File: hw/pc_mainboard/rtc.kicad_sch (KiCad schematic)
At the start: 1 part, among them U5 MCP7940MT-I/SN

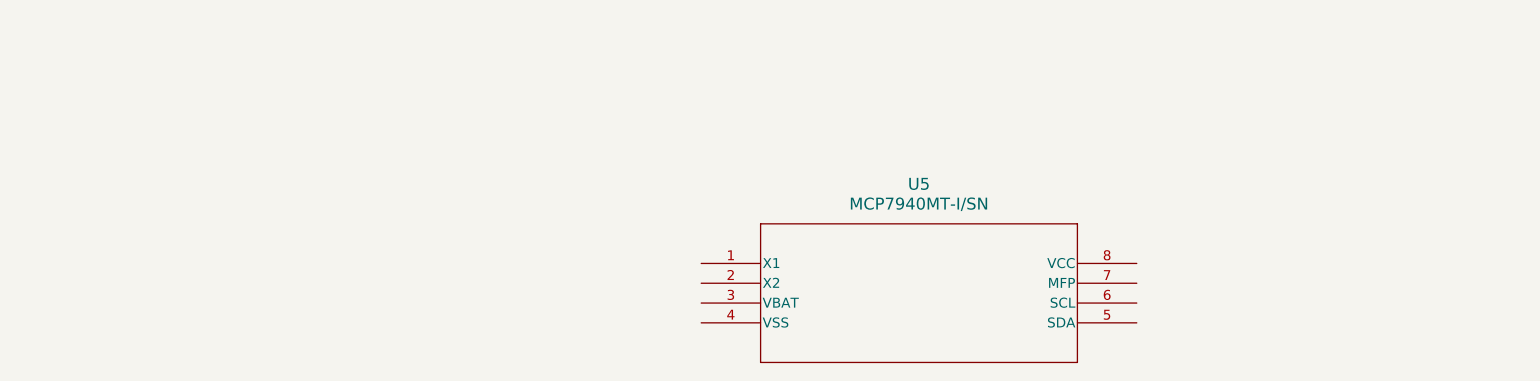
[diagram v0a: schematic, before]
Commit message: RTC Schematic Capture (#35)
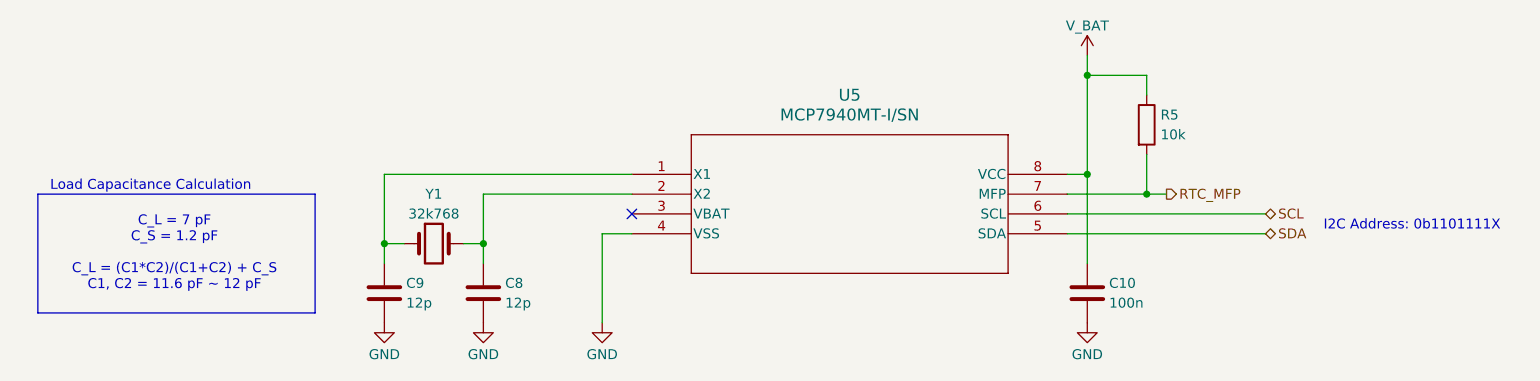
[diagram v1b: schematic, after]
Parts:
- added C10: 100n, symbol Device:C
- added C8, C9: 12p, symbol Device:C
- added R5: 10k, symbol Device:R
- added Y1: 32k768, symbol Device:Crystal
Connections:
- net at U5.1 (X1): now also C9.1, Y1.1
- net at U5.2 (X2): now also C8.1, Y1.2
- net GND: now reaches U5.4 (VSS)
- net GND: now also C10.2, C8.2, C9.2
- net SDA: now reaches U5.5 (SDA)
- net SCL: now reaches U5.6 (SCL)
- net RTC_MFP: now reaches U5.7 (MFP)
- net RTC_MFP: now also R5.2
- net V_BAT: now reaches U5.8 (VCC)
- net V_BAT: now also C10.1, R5.1
- no-connect marks 0 -> 1
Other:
- note added: "C_L = 7 pF C_S = 1.2 pF C_L = (C1*C2)/(C1+C2) + C_S C1, C2 = 11.6 pF ~ 12 pF"
- note added: "I2C Address: 0b1101111X"
- note added: "Load Capacitance Calculation"
- moved on the sheet: U5

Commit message: EEPROM Research (#36)
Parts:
- removed U5: MCP7940MT-I/SN, SOIC8-N_MC_MCH, symbol pc_mainboard:MCP7940MT-I_SN
- added U5: MCP7940MT-I/SN, SOIC8-N_MC_MCH, symbol pc_mainboard:rtc_MCP7940MT-I_SN
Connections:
- net GND: now also U5.4 (VSS)
- net RTC_MFP: now also U5.7 (MFP)
- net SCL: now also U5.6 (SCL)
- net SDA: now also U5.5 (SDA)
- net V_BAT: now also U5.8 (VCC)
- net at C9.1, Y1.1: now also U5.1 (X1)
- net at C8.1, Y1.2: now also U5.2 (X2)
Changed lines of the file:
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@@
+	)
+	(symbol
+		(lib_id "pc_mainboard:rtc_MCP7940MT-I_SN")
+		(at 119.38 88.9 0)
+		(unit 1)
+		(exclude_from_sim no)
+		(in_bom yes)
+		(on_board yes)
+		(dnp no)
+		(fields_autoplaced yes)
+		(property "Reference" "U5"
+			(at 147.32 78.74 0)
+			(effects
+				(font
+					(size 1.524 1.524)
+				)
+			)
+		)
+		(property "Value" "MCP7940MT-I/SN"
+			(at 147.32 81.28 0)
+			(effects
+				(font
+					(size 1.524 1.524)
+				)
+			)
+		)
+		(property "Footprint" "SOIC8-N_MC_MCH"
+			(at 119.38 88.9 0)
+			(effects
+				(font
+					(size 1.27 1.27)
+					(italic yes)
+				)
+				(hide yes)
+			)
+		)
+		(property "Datasheet" "MCP7940MT-I/SN"
+			(at 119.38 88.9 0)
+			(effects
+				(font
+					(size 1.27 1.27)
+					(italic yes)
+				)
+				(hide yes)
+			)
+		)
+		(property "Description" ""
+			(at 119.38 88.9 0)
+			(effects
+				(font
+					(size 1.27 1.27)
+				)
+				(hide yes)
+			)
+		)
+		(pin "4"
+		)
+		(pin "7"
+		)
+		(pin "5"
+		)
+		(pin "8"
+		)
+		(pin "1"
+		)
+		(pin "3"
+		)
+		(pin "6"
+		)
+		(pin "2"
+		)
+		(instances
+			(project ""
+				(path "/69a74940-cd00-4a75-bd5b-2bda9e86219a/01dad65e-16f9-4460-a8fe-f2bb5f9096e6"
+					(reference "U5")
+					(unit 1)
+				)
+			)
+		)
 	)
 	(symbol
@@
 					(unit 1)
 				)
-			)
-		)
-	)
-	(symbol
-		(lib_id "pc_mainboard:MCP7940MT-I_SN")
-		(at 119.38 88.9 0)
-		(unit 1)
-		(exclude_from_sim no)
-		(in_bom yes)
-		(on_board yes)
-		(dnp no)
-		(fields_autoplaced yes)
-		(property "Reference" "U5"
-			(at 147.32 78.74 0)
-			(effects
-				(font
-					(size 1.524 1.524)
-				)
-			)
-		)
-		(property "Value" "MCP7940MT-I/SN"
-			(at 147.32 81.28 0)
-			(effects
-				(font
-					(size 1.524 1.524)
-				)
-			)
-		)
-		(property "Footprint" "SOIC8-N_MC_MCH"
-			(at 119.38 88.9 0)
-			(effects
-				(font
-					(size 1.27 1.27)
-					(italic yes)
-				)
-				(hide yes)
-			)
-		)
-		(property "Datasheet" "MCP7940MT-I/SN"
-			(at 119.38 88.9 0)
-			(effects
-				(font
-					(size 1.27 1.27)
-					(italic yes)
-				)
-				(hide yes)
-			)
-		)
-		(property "Description" ""
-			(at 119.38 88.9 0)
-			(effects
-				(font
-					(size 1.27 1.27)
-				)
-				(hide yes)
-			)
-		)
-		(pin "3"
-		)
-		(pin "1"
-		)
-		(pin "2"
-		)
-		(pin "7"
-		)
-		(pin "6"
-		)
-		(pin "5"
-		)
-		(pin "4"
-		)
-		(pin "8"
-		)
-		(instances
-			(project ""
-				(path "/69a74940-cd00-4a75-bd5b-2bda9e86219a/01dad65e-16f9-4460-a8fe-f2bb5f9096e6"
-					(reference "U5")
-					(unit 1)
-				)

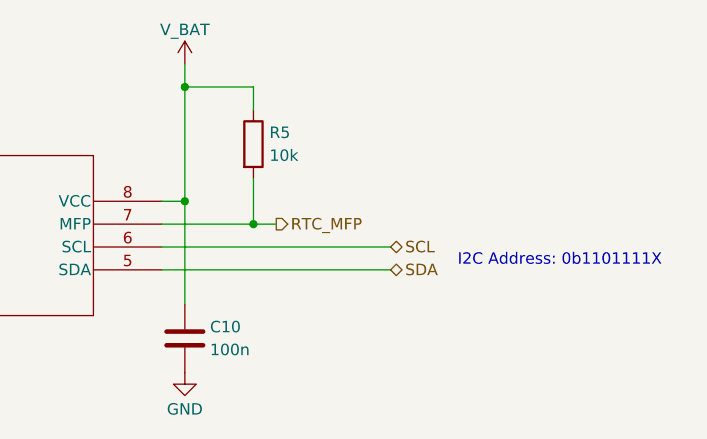
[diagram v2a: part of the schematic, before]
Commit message: RAM Schematic Capture (#39)
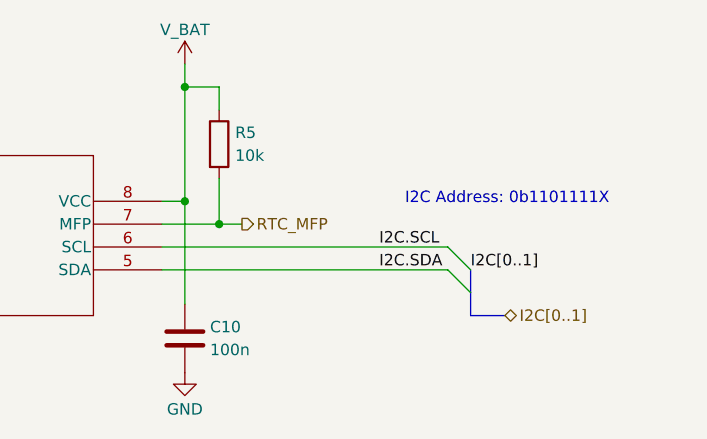
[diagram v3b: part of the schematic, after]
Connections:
- net SCL renamed I2C.SCL
- net SDA renamed I2C.SDA
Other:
- moved on the sheet: R5
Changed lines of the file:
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@@
-	)
-	(junction
-		(at 185.42 91.44)
-		(diameter 0)
-		(color 0 0 0 0)
 	)
 	(junction
@@
 	)
 	(junction
+		(at 181.61 91.44)
+		(diameter 0)
+		(color 0 0 0 0)
+	)
+	(junction
 		(at 100.33 97.79)
 		(diameter 0)
@@
 		(at 119.38 93.98)
 	)
-	(wire
-		(pts
-			(xy 175.26 96.52) (xy 200.66 96.52)
-		)
-		(stroke
-			(width 0)
-			(type default)
-		)
-	)
-	(wire
-		(pts
-			(xy 185.42 78.74) (xy 185.42 76.2)
+	(bus_entry
+		(at 207.01 96.52)
+		(size 2.54 2.54)
+		(stroke
+			(width 0)
+			(type default)
+		)
+	)
+	(bus_entry
+		(at 207.01 93.98)
+		(size 2.54 2.54)
+		(stroke
+			(width 0)
+			(type default)
+		)
+	)
+	(wire
+		(pts
+			(xy 181.61 78.74) (xy 181.61 76.2)
+		)
+		(stroke
+			(width 0)
+			(type default)
+		)
+	)
+	(wire
+		(pts
+			(xy 175.26 96.52) (xy 207.01 96.52)
+		)
+		(stroke
+			(width 0)
+			(type default)
+		)
+	)
+	(wire
+		(pts
+			(xy 175.26 93.98) (xy 207.01 93.98)
 		)
 		(stroke
@@
 	(wire
 		(pts
-			(xy 185.42 76.2) (xy 177.8 76.2)
+			(xy 181.61 76.2) (xy 177.8 76.2)
 		)
 		(stroke
@@
 	(wire
 		(pts
-			(xy 175.26 91.44) (xy 185.42 91.44)
+			(xy 181.61 91.44) (xy 184.15 91.44)
+		)
+		(stroke
+			(width 0)
+			(type default)
+		)
+	)
+	(wire
+		(pts
+			(xy 175.26 91.44) (xy 181.61 91.44)
 		)
 		(stroke
@@
 		)
 	)
+	(bus
+		(pts
+			(xy 209.55 96.52) (xy 209.55 99.06)
+		)
+		(stroke
+			(width 0)
+			(type default)
+		)
+	)
 	(wire
 		(pts
@@
 		)
 	)
-	(wire
-		(pts
-			(xy 175.26 93.98) (xy 200.66 93.98)
+	(bus
+		(pts
+			(xy 209.55 99.06) (xy 209.55 101.6)
 		)
 		(stroke
@@
 	(wire
 		(pts
-			(xy 185.42 91.44) (xy 185.42 86.36)
-		)
-		(stroke
-			(width 0)
-			(type default)
-		)
-	)
-	(wire
-		(pts
-			(xy 185.42 91.44) (xy 187.96 91.44)
+			(xy 181.61 91.44) (xy 181.61 86.36)
 		)
 		(stroke
@@
 		(pts
 			(xy 87.63 97.79) (xy 87.63 88.9)
+		)
+		(stroke
+			(width 0)
+			(type default)
+		)
+	)
+	(bus
+		(pts
+			(xy 209.55 101.6) (xy 213.36 101.6)
 		)
 		(stroke
@@
 	(text "I2C Address: 0b1101111X"
 		(exclude_from_sim no)
-		(at 219.456 95.504 0)
+		(at 213.614 88.646 0)
 		(effects
 			(font
@@
 		)
 	)
-	(hierarchical_label "RTC_MFP"
-		(shape output)
-		(at 187.96 91.44 0)
+	(label "I2C.SDA"
+		(at 199.39 96.52 0)
 		(effects
 			(font
 				(size 1.27 1.27)
 			)
-			(justify left)
-		)
-	)
-	(hierarchical_label "SCL"
-		(shape bidirectional)
-		(at 200.66 93.98 0)
+			(justify left bottom)
+		)
+	)
+	(label "I2C.SCL"
+		(at 199.39 93.98 0)
 		(effects
 			(font
 				(size 1.27 1.27)
 			)
+			(justify left bottom)
+		)
+	)
+	(label "I2C[0..1]"
+		(at 209.55 96.52 0)
+		(effects
+			(font
+				(size 1.27 1.27)
+			)
+			(justify left bottom)
+		)
+	)
+	(hierarchical_label "I2C[0..1]"
+		(shape bidirectional)
+		(at 213.36 101.6 0)
+		(effects
+			(font
+				(size 1.27 1.27)
+			)
 			(justify left)
 		)
 	)
-	(hierarchical_label "SDA"
-		(shape bidirectional)
-		(at 200.66 96.52 0)
+	(hierarchical_label "RTC_MFP"
+		(shape output)
+		(at 184.15 91.44 0)
 		(effects
 			(font
@@
 	(symbol
 		(lib_id "Device:R")
-		(at 185.42 82.55 0)
+		(at 181.61 82.55 0)
 		(unit 1)
 		(exclude_from_sim no)
@@
 		(dnp no)
 		(property "Reference" "R5"
-			(at 187.198 81.28 0)
+			(at 183.388 81.28 0)
 			(effects
 				(font
@@
 		)
 		(property "Value" "10k"
-			(at 187.198 83.8201 0)
+			(at 183.388 83.8201 0)
 			(effects
 				(font
@@
 		)
 		(property "Footprint" ""
-			(at 183.642 82.55 90)
+			(at 179.832 82.55 90)
 			(effects
 				(font
@@
 		)
 		(property "Datasheet" "~"
-			(at 185.42 82.55 0)
+			(at 181.61 82.55 0)
 			(effects
 				(font
@@
 		)
 		(property "Description" "Resistor"
-			(at 185.42 82.55 0)
-			(effects
-				(font
+			(at 181.61 82.55 0)
+			(effects
+				(font
